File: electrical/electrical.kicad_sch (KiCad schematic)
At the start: 0 parts

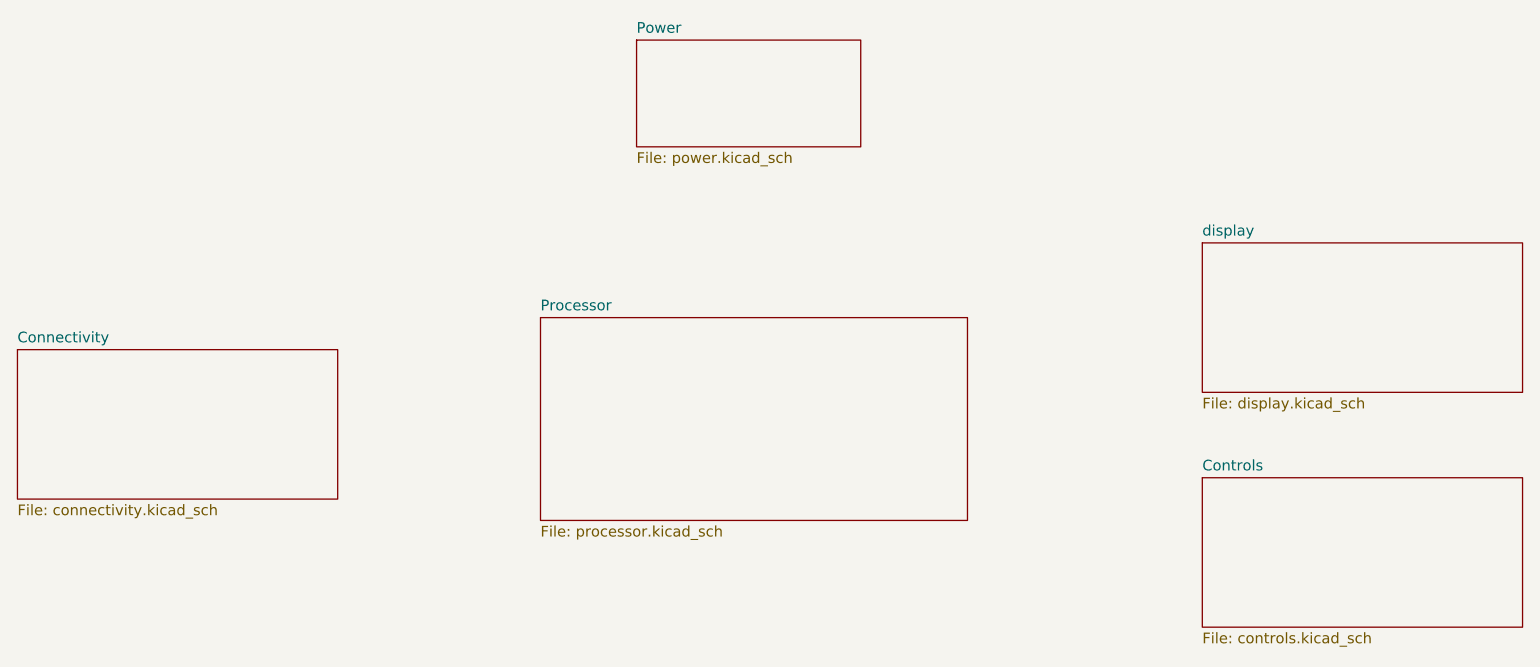
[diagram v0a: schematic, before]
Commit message: #18 Adding decoupling capacitor.
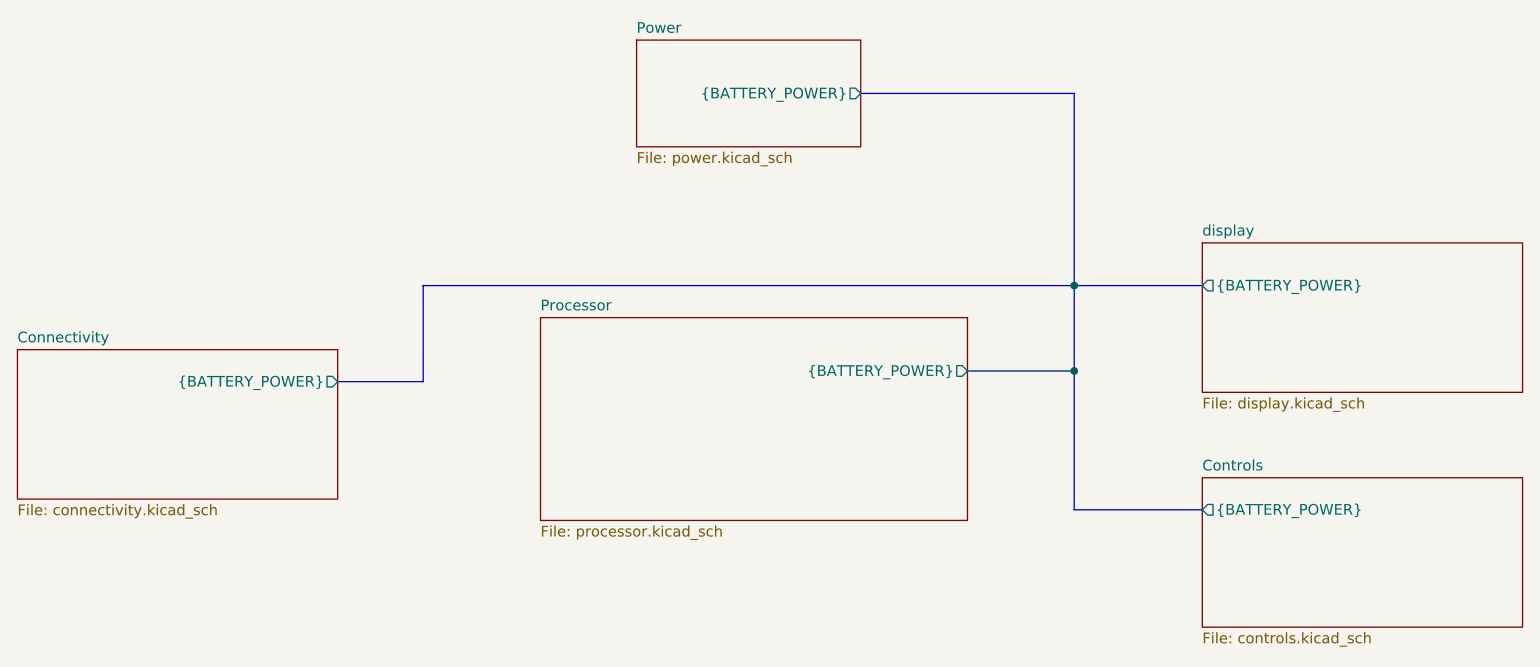
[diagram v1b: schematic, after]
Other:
- sheet Connectivity ports: added {BATTERY_POWER}; removed none
- sheet Controls ports: added {BATTERY_POWER}; removed none
- sheet Power ports: added {BATTERY_POWER}; removed none
- sheet Processor ports: added {BATTERY_POWER}; removed none
- sheet display ports: added {BATTERY_POWER}; removed none
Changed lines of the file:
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@@
 		(company "Alumapower")
+	)
+	(junction
+		(at 179.07 81.28)
+		(diameter 0)
+		(color 0 0 0 0)
+	)
+	(junction
+		(at 179.07 91.44)
+		(diameter 0)
+		(color 0 0 0 0)
+	)
+	(bus
+		(pts
+			(xy 179.07 91.44) (xy 179.07 107.95)
+		)
+		(stroke
+			(width 0)
+			(type default)
+		)
+	)
+	(bus
+		(pts
+			(xy 101.6 92.71) (xy 101.6 81.28)
+		)
+		(stroke
+			(width 0)
+			(type default)
+		)
+	)
+	(bus
+		(pts
+			(xy 179.07 58.42) (xy 179.07 81.28)
+		)
+		(stroke
+			(width 0)
+			(type default)
+		)
+	)
+	(bus
+		(pts
+			(xy 101.6 81.28) (xy 179.07 81.28)
+		)
+		(stroke
+			(width 0)
+			(type default)
+		)
+	)
+	(bus
+		(pts
+			(xy 166.37 91.44) (xy 179.07 91.44)
+		)
+		(stroke
+			(width 0)
+			(type default)
+		)
+	)
+	(bus
+		(pts
+			(xy 179.07 107.95) (xy 194.31 107.95)
+		)
+		(stroke
+			(width 0)
+			(type default)
+		)
+	)
+	(bus
+		(pts
+			(xy 91.44 92.71) (xy 101.6 92.71)
+		)
+		(stroke
+			(width 0)
+			(type default)
+		)
+	)
+	(bus
+		(pts
+			(xy 179.07 81.28) (xy 179.07 91.44)
+		)
+		(stroke
+			(width 0)
+			(type default)
+		)
+	)
+	(bus
+		(pts
+			(xy 179.07 81.28) (xy 194.31 81.28)
+		)
+		(stroke
+			(width 0)
+			(type default)
+		)
+	)
+	(bus
+		(pts
+			(xy 153.67 58.42) (xy 179.07 58.42)
+		)
+		(stroke
+			(width 0)
+			(type default)
+		)
 	)
 	(sheet
@@
 				)
 				(justify left top)
+			)
+		)
+		(pin "{BATTERY_POWER}" output
+			(at 166.37 91.44 0)
+			(effects
+				(font
+					(size 1.27 1.27)
+				)
+				(justify right)
 			)
 		)
@@
 			)
 		)
+		(pin "{BATTERY_POWER}" output
+			(at 194.31 81.28 180)
+			(effects
+				(font
+					(size 1.27 1.27)
+				)
+				(justify left)
+			)
+		)
 		(instances
 			(project "electrical"
@@
 			)
 		)
+		(pin "{BATTERY_POWER}" output
+			(at 194.31 107.95 180)
+			(effects
+				(font
+					(size 1.27 1.27)
+				)
+				(justify left)
+			)
+		)
 		(instances
 			(project "electrical"
@@
 			)
 		)
+		(pin "{BATTERY_POWER}" output
+			(at 91.44 92.71 0)
+			(effects
+				(font
+					(size 1.27 1.27)
+				)
+				(justify right)
+			)
+		)
 		(instances
 			(project "electrical"
@@
 			)
 		)
+		(pin "{BATTERY_POWER}" output
+			(at 153.67 58.42 0)
+			(effects
+				(font
+					(size 1.27 1.27)
+				)
+				(justify right)
+			)
+		)
